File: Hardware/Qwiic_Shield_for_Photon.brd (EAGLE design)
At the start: 43.2 x 35.6 mm, 22 parts

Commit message: ran checklist, pre design review
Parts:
- added FD1, FD2, FD3, FD4: FIDUCIALUFIDUCIAL, SparkFun-Aesthetics:FIDUCIAL-MICRO
- added LOGO2: REVISION, SparkFun-Aesthetics:REVISION
- J1, J2, J3: device SparkX:1X04_1MM_RA -> SparkFun-Connectors:1X04_1MM_RA
- U$1: device SparkX:SPARKX-TINY -> SparkFun-Aesthetics:SFE_LOGO_FLAME_.2
- U$4: value SPARKX-LOGO5 -> SFE_LOGO_NAME.1_INCH; device SparkX:SPARKX-LARGE -> SparkFun-Aesthetics:SFE_LOGO_NAME_.1
- moved FRAME1 7.62 mm to (-11.4, -20.3)
- moved U$4 5.58 mm to (42.7, 23.1), turned to 270 degrees
- moved U$1 1.44 mm to (36.6, 2.29)
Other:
- board text added: "Andy England"
- board text added: "v01"
- board text removed: "X10"
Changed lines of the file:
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@@
 <?xml version="1.0" encoding="utf-8"?>
 <!DOCTYPE eagle SYSTEM "eagle.dtd">
-<eagle version="7.6.0">
+<eagle version="7.7.0">
 <drawing>
 <settings>
@@
 <layer number="37" name="tTest" color="7" fill="1" visible="no" active="yes"/>
 <layer number="38" name="bTest" color="7" fill="1" visible="no" active="yes"/>
-<layer number="39" name="tKeepout" color="4" fill="11" visible="no" active="yes"/>
-<layer number="40" name="bKeepout" color="1" fill="11" visible="no" active="yes"/>
+<layer number="39" name="tKeepout" color="4" fill="11" visible="yes" active="yes"/>
+<layer number="40" name="bKeepout" color="1" fill="11" visible="yes" active="yes"/>
 <layer number="41" name="tRestrict" color="4" fill="10" visible="no" active="yes"/>
 <layer number="42" name="bRestrict" color="1" fill="10" visible="no" active="yes"/>
@@
 <layer number="45" name="Holes" color="7" fill="1" visible="yes" active="yes"/>
 <layer number="46" name="Milling" color="3" fill="1" visible="no" active="yes"/>
-<layer number="47" name="Measures" color="7" fill="1" visible="no" active="yes"/>
+<layer number="47" name="Measures" color="7" fill="1" visible="yes" active="yes"/>
 <layer number="48" name="Document" color="7" fill="1" visible="no" active="yes"/>
 <layer number="49" name="Reference" color="7" fill="1" visible="yes" active="yes"/>
@@
 <layer number="230" name="230bmp" color="7" fill="1" visible="no" active="yes"/>
 <layer number="231" name="231bmp" color="7" fill="1" visible="no" active="yes"/>
+<layer number="232" name="Eagle3D_PG2" color="7" fill="1" visible="yes" active="yes"/>
+<layer number="233" name="Eagle3D_PG3" color="7" fill="1" visible="yes" active="yes"/>
 <layer number="248" name="Housing" color="7" fill="1" visible="no" active="yes"/>
 <layer number="249" name="Edge" color="7" fill="1" visible="no" active="yes"/>
@@
 <text x="26.67" y="27.94" size="1.016" layer="22" font="vector" ratio="15" rot="MR0">3V3</text>
 <text x="13.843" y="33.909" size="1.016" layer="21" font="vector" ratio="15">I2C</text>
-<text x="8.128" y="0.381" size="1.016" layer="16" font="vector" ratio="15" rot="MR0">X10</text>
+<text x="9.398" y="0.381" size="1.27" layer="16" font="vector" ratio="15" rot="MR0">v01</text>
 <wire x1="19.304" y1="28.448" x2="20.828" y2="28.448" width="0.2032" layer="21"/>
 <wire x1="20.828" y1="28.448" x2="21.463" y2="29.083" width="0.2032" layer="21"/>
@@
 <wire x1="28.575" y1="28.448" x2="29.21" y2="29.083" width="0.2032" layer="22"/>
 <text x="16.002" y="33.909" size="1.016" layer="22" font="vector" ratio="15" rot="MR0">I2C</text>
-<text x="19.05" y="-12.7" size="1.778" layer="51" font="vector" ratio="10">Joel Bartlett</text>
+<text x="19.05" y="-20.32" size="1.778" layer="51" font="vector">Joel Bartlett</text>
 <wire x1="15.24" y1="31.75" x2="27.432" y2="31.75" width="0.2032" layer="21"/>
 <wire x1="27.432" y1="35.56" x2="27.305" y2="35.56" width="0.2032" layer="21"/>
@@
 <wire x1="13.97" y1="31.75" x2="13.97" y2="29.21" width="0.254" layer="22"/>
 <wire x1="21.59" y1="29.21" x2="21.59" y2="31.75" width="0.254" layer="22"/>
+<text x="19.05" y="-22.86" size="1.778" layer="51">Andy England</text>
+<dimension x1="0" y1="0" x2="43.18" y2="0" x3="21.59" y3="-10.16" textsize="0.8128" textratio="15" layer="47" unit="inch"/>
 </plain>
 <attributes>
@@
 </autorouter>
 <elements>
-<element name="FRAME1" library="SparkFun-Aesthetics" package="CREATIVE_COMMONS" value="FRAME-LETTER" x="-11.43" y="-12.7"/>
+<element name="FRAME1" library="SparkFun-Aesthetics" package="CREATIVE_COMMONS" value="FRAME-LETTER" x="-11.43" y="-20.32"/>
 <element name="JP1" library="SparkFun-Boards" package="PARTICLE_PHOTON_TEMPLATE_NO_STANDOFF" value="PARTICLE_PHOTONTEMPLATE_NO_STANDOFF" x="21.59" y="19.05"/>
 <element name="JP2" library="SparkFun-Connectors" package="1X04" value="" x="17.78" y="34.29"/>
@@
 <element name="JP9" library="SparkFun-Connectors" package="1X09_NO_SILK" value="" x="25.4" y="6.35" rot="R90"/>
 <element name="JP10" library="SparkFun-Connectors" package="1X09_NO_SILK" value="" x="27.94" y="6.35" rot="R90"/>
-<element name="J1" library="SparkX" package="1X04_1MM_RA" value="" x="5.08" y="11.43" rot="R270"/>
-<element name="J2" library="SparkX" package="1X04_1MM_RA" value="" x="38.1" y="24.13" rot="R90"/>
-<element name="J3" library="SparkX" package="1X04_1MM_RA" value="" x="38.1" y="11.43" rot="R90"/>
+<element name="J1" library="SparkFun-Connectors" package="1X04_1MM_RA" value="" x="5.08" y="11.43" rot="R270">
+<attribute name="PROD_ID" value="CONN-13694" x="5.08" y="11.43" size="1.778" layer="27" rot="R270" display="off"/>
+<attribute name="VALUE" value="" x="5.08" y="11.43" size="1.778" layer="27" rot="R270" display="off"/>
+</element>
+<element name="J2" library="SparkFun-Connectors" package="1X04_1MM_RA" value="" x="38.1" y="24.13" rot="R90">
+<attribute name="PROD_ID" value="CONN-13694" x="38.1" y="24.13" size="1.778" layer="27" rot="R90" display="off"/>
+<attribute name="VALUE" value="" x="38.1" y="24.13" size="1.778" layer="27" rot="R90" display="off"/>
+</element>
+<element name="J3" library="SparkFun-Connectors" package="1X04_1MM_RA" value="" x="38.1" y="11.43" rot="R90">
+<attribute name="PROD_ID" value="CONN-13694" x="38.1" y="11.43" size="1.778" layer="27" rot="R90" display="off"/>
+<attribute name="VALUE" value="" x="38.1" y="11.43" size="1.778" layer="27" rot="R90" display="off"/>
+</element>
 <element name="J4" library="SparkX" package="1X04_1MM_RA" value="" x="5.08" y="24.13" rot="R270"/>
 <element name="H1" library="SparkFun-Hardware" package="STAND-OFF" value="STAND-OFF" x="40.64" y="2.54"/>
@@
 <element name="H3" library="SparkFun-Hardware" package="STAND-OFF" value="STAND-OFF" x="2.54" y="2.54"/>
 <element name="H4" library="SparkFun-Hardware" package="STAND-OFF" value="STAND-OFF" x="2.54" y="33.02"/>
-<element name="U$1" library="SparkX" package="SPARKX-TINY" value="" x="35.56" y="1.27"/>
+<element name="U$1" library="SparkFun-Aesthetics" package="SFE_LOGO_FLAME_.2" value="" x="36.576" y="2.286"/>
 <element name="LOGO1" library="SparkFun-Aesthetics" package="OSHW-LOGO-M" value="OSHW-LOGOM" x="2.54" y="17.78" rot="MR90"/>
-<element name="U$4" library="SparkX" package="SPARKX-LARGE" value="SPARKX-LOGO5" x="41.021" y="17.78" rot="MR90"/>
+<element name="U$4" library="SparkFun-Aesthetics" package="SFE_LOGO_NAME_.1" value="SFE_LOGO_NAME.1_INCH" x="42.672" y="23.114" rot="MR270"/>
+<element name="FD1" library="SparkFun-Aesthetics" package="FIDUCIAL-MICRO" value="FIDUCIALUFIDUCIAL" x="6.35" y="5.08"/>
+<element name="FD2" library="SparkFun-Aesthetics" package="FIDUCIAL-MICRO" value="FIDUCIALUFIDUCIAL" x="6.35" y="5.08" rot="MR0"/>
+<element name="FD3" library="SparkFun-Aesthetics" package="FIDUCIAL-MICRO" value="FIDUCIALUFIDUCIAL" x="35.56" y="34.29"/>
+<element name="FD4" library="SparkFun-Aesthetics" package="FIDUCIAL-MICRO" value="FIDUCIALUFIDUCIAL" x="35.56" y="34.29" rot="MR0"/>
+<element name="LOGO2" library="SparkFun-Aesthetics" package="REVISION" value="REVISION" x="0" y="-22.86"/>
 </elements>
 <signals>

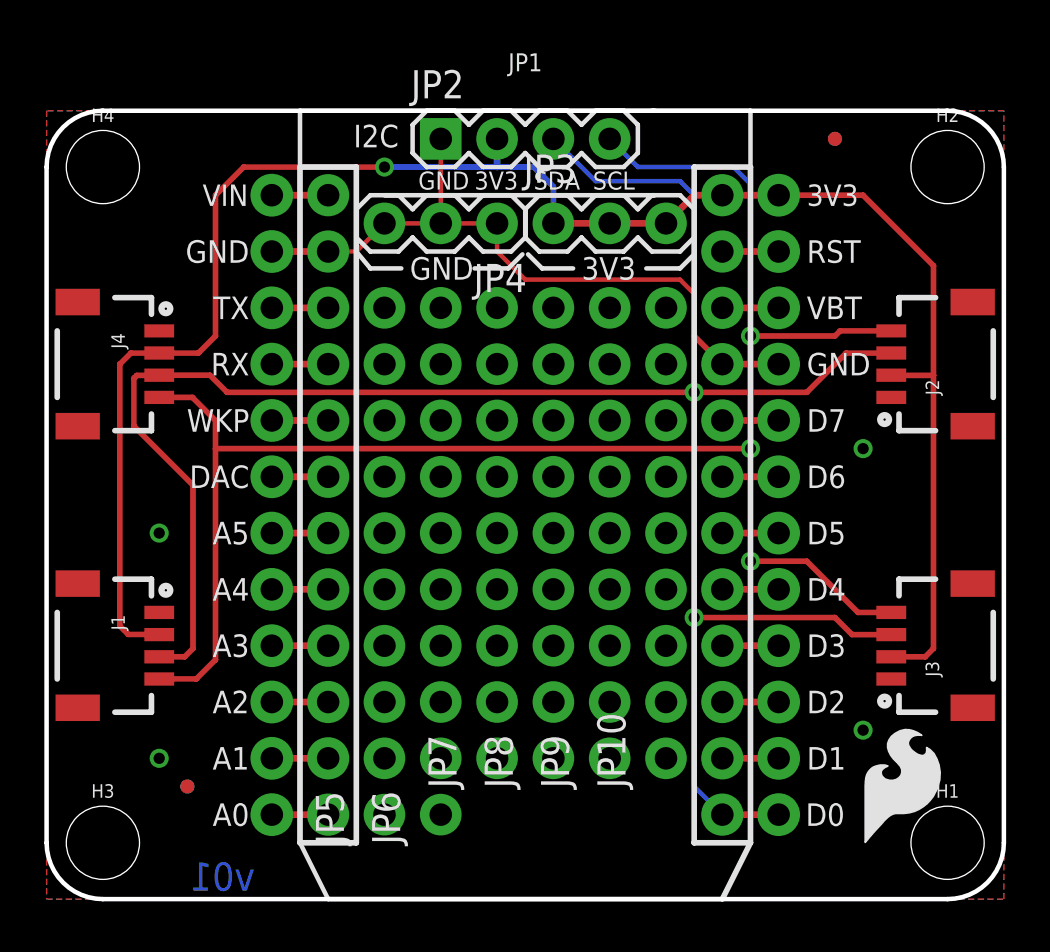
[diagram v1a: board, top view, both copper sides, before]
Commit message: updated version silk, added gnd stitching
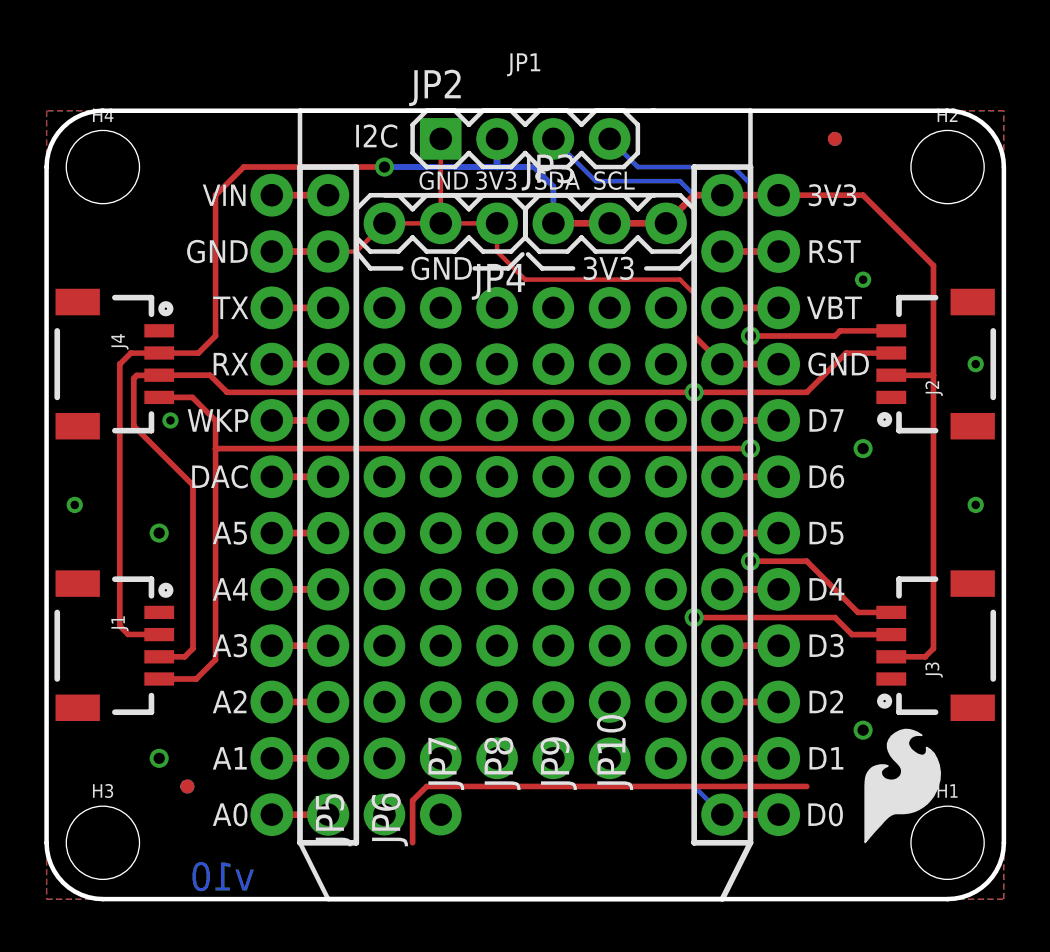
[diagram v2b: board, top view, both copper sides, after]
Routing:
- net GND: track 26.6 -> 46.6 mm, vias 4 -> 9
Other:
- board text added: "v10"
- board text removed: "v01"
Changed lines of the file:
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@@
 <text x="26.67" y="27.94" size="1.016" layer="22" font="vector" ratio="15" rot="MR0">3V3</text>
 <text x="13.843" y="33.909" size="1.016" layer="21" font="vector" ratio="15">I2C</text>
-<text x="9.398" y="0.381" size="1.27" layer="16" font="vector" ratio="15" rot="MR0">v01</text>
+<text x="9.398" y="0.381" size="1.27" layer="16" font="vector" ratio="15" rot="MR0">v10</text>
 <wire x1="19.304" y1="28.448" x2="20.828" y2="28.448" width="0.2032" layer="21"/>
 <wire x1="20.828" y1="28.448" x2="21.463" y2="29.083" width="0.2032" layer="21"/>
@@
 <via x="5.08" y="16.51" extent="1-16" drill="0.508"/>
 <via x="5.08" y="6.35" extent="1-16" drill="0.508"/>
+<via x="36.83" y="27.94" extent="1-16" drill="0.381"/>
+<via x="41.91" y="17.78" extent="1-16" drill="0.381"/>
+<wire x1="16.51" y1="2.54" x2="16.51" y2="4.445" width="0.254" layer="1"/>
+<wire x1="16.51" y1="4.445" x2="17.145" y2="5.08" width="0.254" layer="1"/>
+<wire x1="17.145" y1="5.08" x2="34.29" y2="5.08" width="0.254" layer="1"/>
+<via x="41.91" y="24.13" extent="1-16" drill="0.381"/>
+<via x="5.588" y="21.59" extent="1-16" drill="0.381"/>
+<via x="1.27" y="17.78" extent="1-16" drill="0.381"/>
 </signal>
 <signal name="VIN">
